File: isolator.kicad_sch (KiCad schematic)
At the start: 43 parts, among them J1 HOST, J2 PORT, Q1 2N7002, T1 750313638, U1 ADuM4165, U2 USBLC6-2SC6, U3 USBLC6-2SC6, U4 SN6505BDBV, U5 TLV76750DGNR, U6 TPS2553DBV, Y1 24M 8pF

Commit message: feat(pcb): host-side routing, U2 channel swap, Gate 3
Routing done in pcbnew by the operator: 157 tracks, 32 vias on F.Cu/B.Cu
covering VBUS_HOST, HOST_D+/-, GND1, PP_A/B, XTALIN/XTALOUT, VDD1 and the J1 CC
pair. Isolated side is not routed yet.

Schematic change, verified rather than assumed: D+ and D- were swapped through
U2's two ESD channels. HOST_D+ moves from U2 pins 1/6 to 3/4 and HOST_D- the
reverse. Endpoints are unchanged -- J1.A6/B6 -> U1.8 is still D+ -- so this is
electrically equivalent (the USBLC6-2SC6's channels are identical) and still
satisfies the in-line 1/3 -> 6/4 requirement of constraint 3, with the channels
exchanged. It is a deliberate rewire, not a library artifact: U3 is the same
part and its /PORT_D+/- nets are unchanged, whereas a symbol pin renumber would
have moved both.

KiCad also rewrote the lib_symbols cache on save (Device:C_Small -> Device:C and
similar), which accounts for the bulk of the schematic diff. ERC is unchanged:
0 errors, still exactly one lib_symbol_mismatch warning on U4.

Gate 3 on the routed host pair: skew 0.0517 mm against a 0.15 mm limit, Zdiff
96.28 ohm against 90 +/-10%. Passing, but at the high end of the band.

Co-Authored-By: Claude Opus 5 <noreply@anthropic.com>
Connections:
- net HOST_D+: now also U2.3 (I/O2), U2.4 (I/O2); no longer U2.1 (I/O1), U2.6 (I/O1)
- net HOST_D-: now also U2.1 (I/O1), U2.6 (I/O1); no longer U2.3 (I/O2), U2.4 (I/O2)

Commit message: wip: operator's mounting holes and fiducials, schematic and board edits
Snapshot of hand work done in KiCad before any repositioning, so it cannot be
lost. Adds H1-H4 (MountingHole_3.2mm_M3_Pad_Via) and FID1-FID4
(Fiducial_0.5mm_Mask1.5mm), currently parked off-board around x=212..251,
plus the corresponding schematic changes.

Also drops a stray ~isolator.kicad_pro.lck that had been committed, and
gitignores that pattern.

Committed as-is, unreviewed. Verification follows in the next commit.

Co-Authored-By: Claude Opus 5 <noreply@anthropic.com>
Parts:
- added FID1, FID2, FID3, FID4: Fiducial, Fiducial:Fiducial_0.5mm_Mask1.5mm, symbol Mechanical:Fiducial
- added H1, H2, H3, H4: MountingHole_Pad, MountingHole:MountingHole_3.2mm_M3_Pad_Via, symbol Mechanical:MountingHole_Pad
- C1, C10, C11, C12, C13, C14, C15, C2, C3, C4, C5, C6, C7, C8, C9, D3, D4, R1, R10, R2, R3, R4, R5, R6, R7, R8, R9: KiLib_Generator (none) -> SMD_2terminal_chip_molded
- J2: value PORT -> ISO_PORT
- Q1, U2, U3, U4, U5, U6: KiLib_Generator (none) -> package/gullwing
- Y1: KiLib_Generator (none) -> crystal_resonator_oscillator; private KLC_S4.1 -> (none)
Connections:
- net GND1: now also H1.1, H2.1
- net GND2: now also H3.1, H4.1

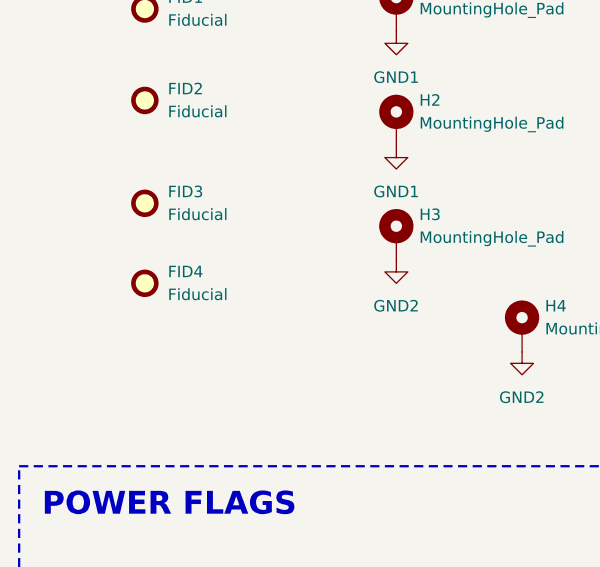
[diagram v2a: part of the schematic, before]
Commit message: feat(pcb): drop to three fiducials in an L, breaking the orientation ambiguity
Four fiducials in symmetric corners have 180-degree rotational symmetry, so the
pattern is identical on a board mounted the wrong way round and gives the placer
no orientation reference. Three corners of a rectangle cannot be rotationally
symmetric, so removing one fixes that by construction rather than by an offset a
"best 3 of 4" fit could undo.

Three is also what the process wants: two fiducials give X, Y and rotation, the
third adds scale/stretch correction and a consistency check. A fourth adds
nothing. Removing one costs no triangulation baseline either -- any three corners
of a rectangle enclose the same area.

FID4 (bottom-right) removed, leaving an L: FID1 (7.50, 2.75), FID2 (7.50, 47.25),
FID3 (112.50, 2.75), with 44.5 / 105.0 / 114.0 mm separations. Numbering stays
contiguous.

Removed from the schematic as well as the board, since the fiducials are real
schematic symbols here -- deleting only the footprint would have broken parity.
Netlist diff is exactly one component: FID4 out, nothing else changed.

ERC 0 errors 0 warnings; DRC 0 violations, 0 unconnected, 0 schematic parity.
Gates 1 and 2 PASS.

Co-Authored-By: Claude Opus 5 <noreply@anthropic.com>
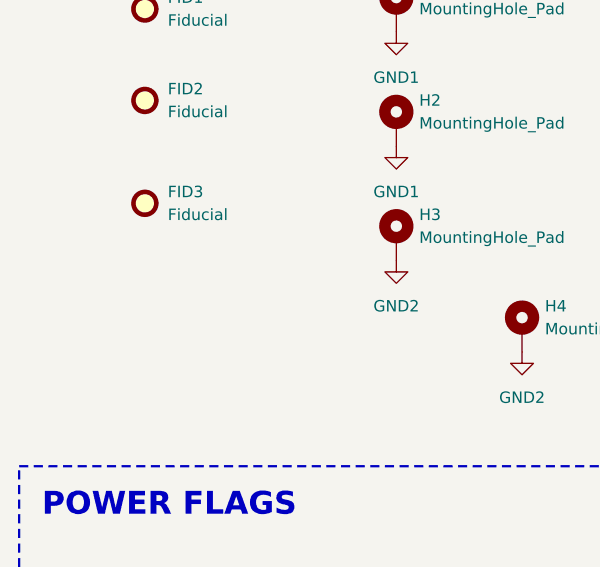
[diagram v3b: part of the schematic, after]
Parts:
- removed FID4: Fiducial, Fiducial:Fiducial_0.5mm_Mask1.5mm, symbol Mechanical:Fiducial
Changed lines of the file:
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@@
-	)
-	(symbol
-		(lib_id "Mechanical:Fiducial")
-		(at 29.21 204.47 0)
-		(unit 1)
-		(body_style 1)
-		(exclude_from_sim no)
-		(in_bom no)
-		(on_board yes)
-		(in_pos_files yes)
-		(dnp no)
-		(fields_autoplaced yes)
-		(property "Reference" "FID4"
-			(at 31.75 203.1999 0)
-			(show_name no)
-			(do_not_autoplace no)
-			(effects
-				(font
-					(size 1.27 1.27)
-				)
-				(justify left)
-			)
-		)
-		(property "Value" "Fiducial"
-			(at 31.75 205.7399 0)
-			(show_name no)
-			(do_not_autoplace no)
-			(effects
-				(font
-					(size 1.27 1.27)
-				)
-				(justify left)
-			)
-		)
-		(property "Footprint" "Fiducial:Fiducial_0.5mm_Mask1.5mm"
-			(at 29.21 204.47 0)
-			(hide yes)
-			(show_name no)
-			(do_not_autoplace no)
-			(effects
-				(font
-					(size 1.27 1.27)
-				)
-			)
-		)
-		(property "Datasheet" ""
-			(at 29.21 204.47 0)
-			(hide yes)
-			(show_name no)
-			(do_not_autoplace no)
-			(effects
-				(font
-					(size 1.27 1.27)
-				)
-			)
-		)
-		(property "Description" "Fiducial Marker"
-			(at 29.21 204.47 0)
-			(hide yes)
-			(show_name no)
-			(do_not_autoplace no)
-			(effects
-				(font
-					(size 1.27 1.27)
-				)
-			)
-		)
-		(instances
-			(project "isolator"
-				(path "/00000000-0000-0000-0000-000000000001"
-					(reference "FID4")
-					(unit 1)
-				)
-			)
-		)
 	)
 	(symbol
